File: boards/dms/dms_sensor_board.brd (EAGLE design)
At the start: 49.5 x 44.5 mm, 33 parts, among them Q1 IRLML5203, Q2 IRLML5203, Q3 IRLML5203, Q4 IRLML5203

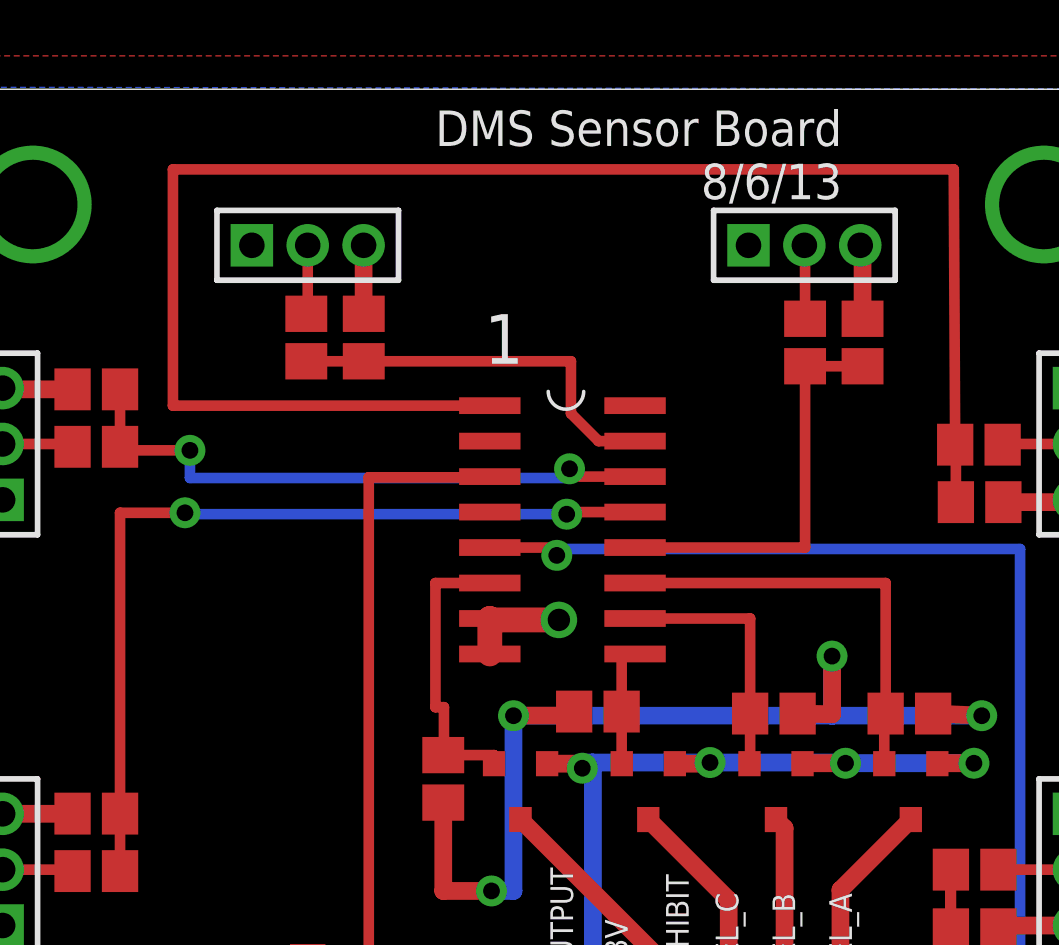
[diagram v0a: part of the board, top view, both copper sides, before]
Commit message: Fixed Mux padsize, cleared relavent DRC errors
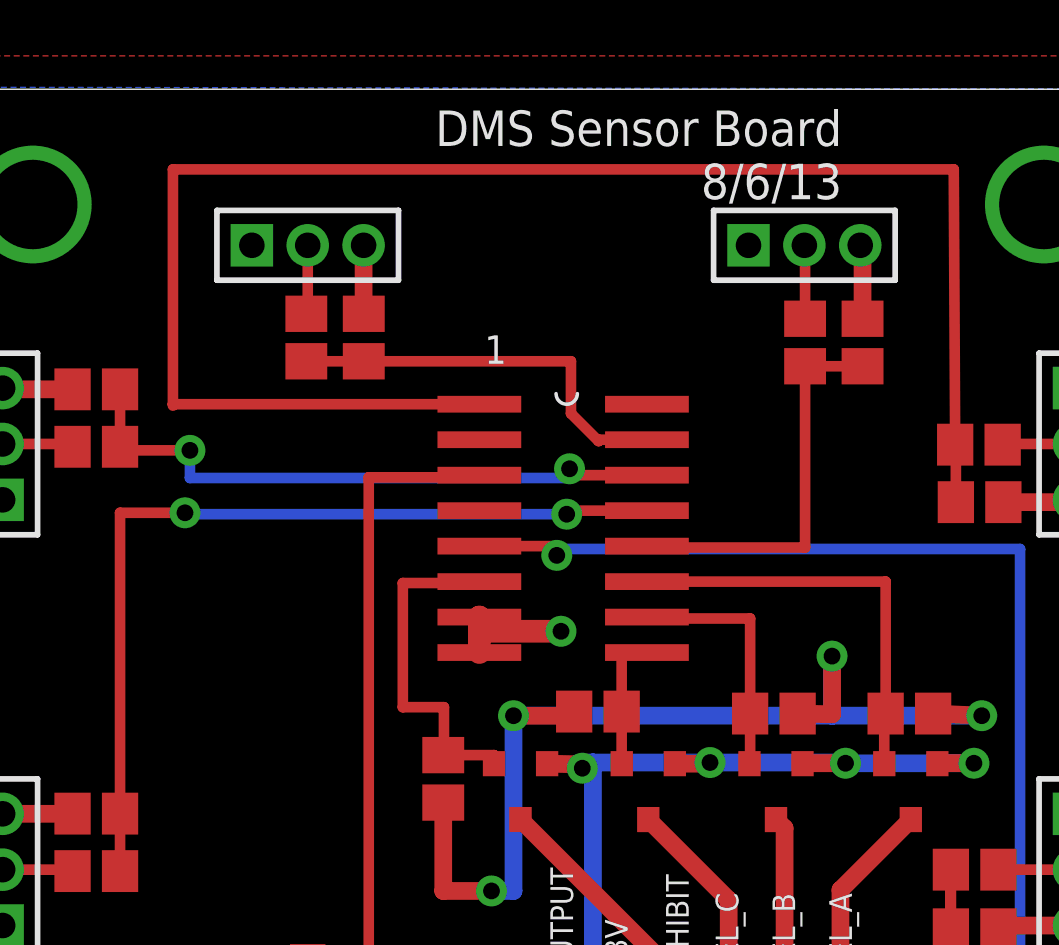
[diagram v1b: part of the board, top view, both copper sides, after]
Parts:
- removed MUX1: 8X1, ngohara_parts:SO16
- added U$1: MUX16BANALOG, wolfbot_specific_parts:SO16
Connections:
- net 5V: now also U$1.16; no longer MUX1.16
- net A_H: now also U$1.11; no longer MUX1.11
- net B_H: now also U$1.10; no longer MUX1.10
- net C_H: now also U$1.9; no longer MUX1.9
- net DATA1-L: now also U$1.13; no longer MUX1.13
- net DATA2-L: now also U$1.14; no longer MUX1.14
- net DATA3-L: now also U$1.15; no longer MUX1.15
- net DATA4-L: now also U$1.12; no longer MUX1.12
- net DATA5-L: now also U$1.1; no longer MUX1.1
- net DATA6-L: now also U$1.5; no longer MUX1.5
- net GND: now also U$1.7, U$1.8; no longer MUX1.7, MUX1.8
- net IH_H: now also U$1.6; no longer MUX1.6
- net N$5: now also U$1.3; no longer MUX1.3
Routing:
- net IH_H: track 10.5 -> 12.6 mm
- net GND: track 25.7 -> 26.5 mm
- net DATA6-L: track 45.3 -> 46.0 mm
- net DATA2-L: track 22.2 -> 22.9 mm
- net DATA1-L: track 31.4 -> 31.9 mm

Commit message: Cleanup issues, working on powerboard res move
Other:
- board text added: "DMS 000"
- board text added: "DMS 060"
- board text added: "DMS 120"
- board text added: "DMS 180"
- board text added: "DMS 240"
- board text added: "DMS 300"
- board text added: "DMS Sensor Board v2013/09/26"
- board text removed: "DMS Sensor Board 8/6/13"
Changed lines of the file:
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@@
 <text x="31.4198" y="12.6492" size="0.8128" layer="25" font="vector" rot="R90">SEL_B</text>
 <text x="33.0962" y="43.688" size="1.27" layer="25" font="vector" rot="R180">DMS Sensor Board
-    8/6/13</text>
+  v2013/09/26</text>
 <text x="20.2946" y="34.6202" size="1.016" layer="25" font="vector">1</text>
 <text x="25.4254" y="12.446" size="0.8128" layer="25" font="vector" rot="R90">3.3V</text>
+<text x="-0.1016" y="10.9728" size="1.27" layer="21">DMS 000</text>
+<text x="-0.7366" y="26.0858" size="1.27" layer="21">DMS 060</text>
+<text x="10.3378" y="35.5092" size="1.27" layer="21" rot="R90">DMS 120</text>
+<text x="37.8968" y="35.7886" size="1.27" layer="21" rot="R90">DMS 180</text>
+<text x="38.0746" y="25.4508" size="1.27" layer="21">DMS 240</text>
+<text x="38.4302" y="10.5156" size="1.27" layer="21">DMS 300</text>
 </plain>
 <attributes>
